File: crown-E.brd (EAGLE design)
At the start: 57.8 x 50.8 mm, 85 parts

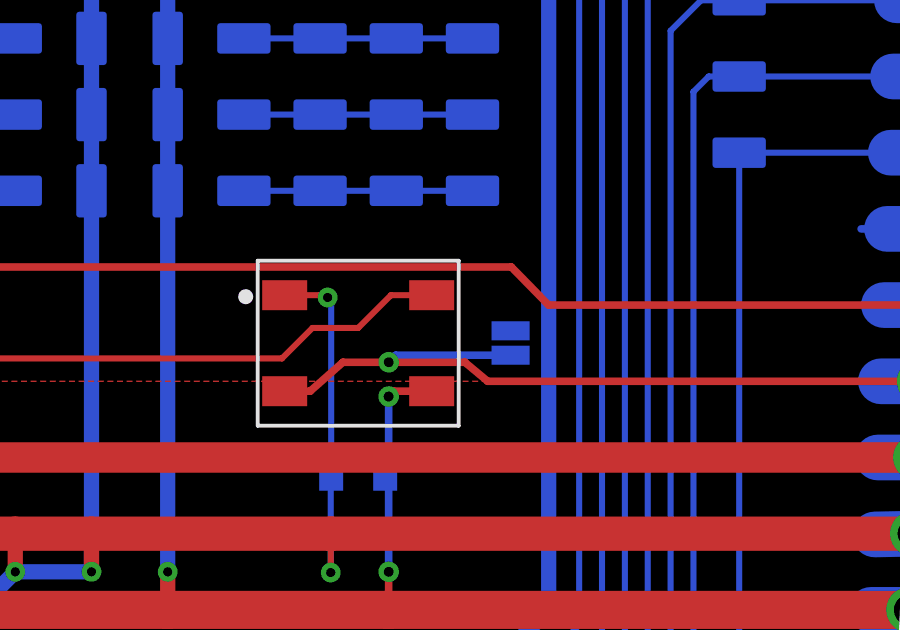
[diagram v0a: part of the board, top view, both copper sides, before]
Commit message: forgot a connection on skip-smd bits
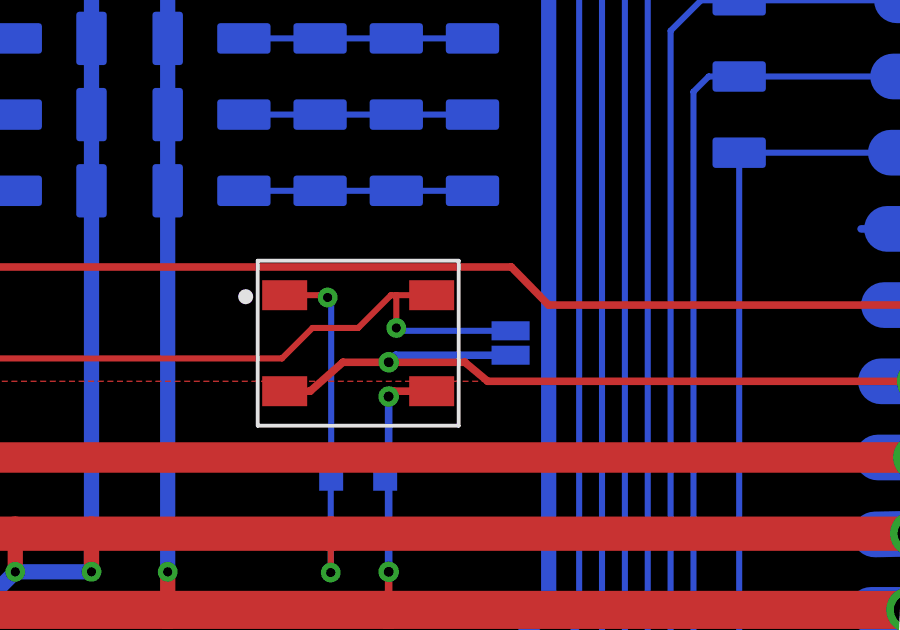
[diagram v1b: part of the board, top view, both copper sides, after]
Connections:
- net N$10: now also SKIP-SMD2.2
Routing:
- net N$10: track 28.2 -> 33.2 mm, vias 1 -> 2
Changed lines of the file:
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@@
 <grid distance="10" unitdist="mil" unit="mil" style="lines" multiple="5" display="yes" altdistance="1" altunitdist="mil" altunit="mil"/>
 <layers>
-<layer number="1" name="Top" color="4" fill="1" visible="no" active="yes"/>
-<layer number="16" name="Bottom" color="1" fill="1" visible="no" active="yes"/>
-<layer number="17" name="Pads" color="2" fill="1" visible="no" active="yes"/>
-<layer number="18" name="Vias" color="2" fill="1" visible="no" active="yes"/>
-<layer number="19" name="Unrouted" color="6" fill="1" visible="no" active="yes"/>
-<layer number="20" name="Dimension" color="15" fill="1" visible="no" active="yes"/>
-<layer number="21" name="tPlace" color="16" fill="1" visible="no" active="yes"/>
-<layer number="22" name="bPlace" color="14" fill="1" visible="no" active="yes"/>
-<layer number="23" name="tOrigins" color="15" fill="1" visible="no" active="yes"/>
-<layer number="24" name="bOrigins" color="15" fill="1" visible="no" active="yes"/>
+<layer number="1" name="Top" color="4" fill="1" visible="yes" active="yes"/>
+<layer number="16" name="Bottom" color="1" fill="1" visible="yes" active="yes"/>
+<layer number="17" name="Pads" color="2" fill="1" visible="yes" active="yes"/>
+<layer number="18" name="Vias" color="2" fill="1" visible="yes" active="yes"/>
+<layer number="19" name="Unrouted" color="6" fill="1" visible="yes" active="yes"/>
+<layer number="20" name="Dimension" color="15" fill="1" visible="yes" active="yes"/>
+<layer number="21" name="tPlace" color="16" fill="1" visible="yes" active="yes"/>
+<layer number="22" name="bPlace" color="14" fill="1" visible="yes" active="yes"/>
+<layer number="23" name="tOrigins" color="15" fill="1" visible="yes" active="yes"/>
+<layer number="24" name="bOrigins" color="15" fill="1" visible="yes" active="yes"/>
 <layer number="25" name="tNames" color="7" fill="1" visible="no" active="yes"/>
 <layer number="26" name="bNames" color="7" fill="1" visible="no" active="yes"/>
@@
 <layer number="28" name="bValues" color="7" fill="1" visible="no" active="yes"/>
 <layer number="29" name="tStop" color="7" fill="3" visible="yes" active="yes"/>
-<layer number="30" name="bStop" color="7" fill="6" visible="no" active="yes"/>
+<layer number="30" name="bStop" color="7" fill="6" visible="yes" active="yes"/>
 <layer number="31" name="tCream" color="7" fill="4" visible="no" active="yes"/>
 <layer number="32" name="bCream" color="7" fill="5" visible="no" active="yes"/>
@@
 <layer number="43" name="vRestrict" color="2" fill="10" visible="no" active="yes"/>
 <layer number="44" name="Drills" color="7" fill="1" visible="no" active="yes"/>
-<layer number="45" name="Holes" color="7" fill="1" visible="no" active="yes"/>
+<layer number="45" name="Holes" color="7" fill="1" visible="yes" active="yes"/>
 <layer number="46" name="Milling" color="3" fill="1" visible="no" active="yes"/>
 <layer number="47" name="Measures" color="7" fill="1" visible="no" active="yes"/>
@@
 <layer number="49" name="Reference" color="7" fill="1" visible="no" active="yes"/>
 <layer number="50" name="dxf" color="7" fill="1" visible="no" active="no"/>
-<layer number="51" name="tDocu" color="6" fill="1" visible="no" active="yes"/>
+<layer number="51" name="tDocu" color="6" fill="1" visible="yes" active="yes"/>
 <layer number="52" name="bDocu" color="7" fill="1" visible="no" active="yes"/>
 <layer number="53" name="tGND_GNDA" color="7" fill="9" visible="no" active="no"/>
@@
 <wire x1="36.576" y1="17.018" x2="38.1" y2="17.018" width="0.2032" layer="1"/>
 <wire x1="38.1" y1="17.018" x2="39.192" y2="18.11" width="0.2032" layer="1"/>
-<wire x1="39.192" y1="18.11" x2="40.55" y2="18.11" width="0.2032" layer="1"/>
+<wire x1="39.192" y1="18.11" x2="39.37" y2="18.11" width="0.2032" layer="1"/>
+<wire x1="39.37" y1="18.11" x2="40.55" y2="18.11" width="0.2032" layer="1"/>
 <wire x1="24.892" y1="16.3631" x2="24.7849" y2="16.256" width="0.2032" layer="16"/>
 <wire x1="24.7849" y1="16.256" x2="21.336" y2="16.256" width="0.2032" layer="16"/>
 <wire x1="21.336" y1="16.256" x2="21.082" y2="16.002" width="0.2032" layer="16"/>
 <via x="21.082" y="16.002" extent="1-16" drill="0.3048"/>
+<contactref element="SKIP-SMD2" pad="2"/>
+<wire x1="43.18" y1="16.9227" x2="39.4653" y2="16.9227" width="0.2032" layer="16"/>
+<wire x1="39.4653" y1="16.9227" x2="39.37" y2="17.018" width="0.2032" layer="16"/>
+<via x="39.37" y="17.018" extent="1-16" drill="0.3048"/>
+<wire x1="39.37" y1="17.018" x2="39.37" y2="18.11" width="0.2032" layer="1"/>
 </signal>
 <signal name="A0">

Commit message: fixed incorrect resistor value
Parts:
- moved PTH-END-NODE 30.8 mm to (13.7, 48.3), turned to 0 degrees
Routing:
- net PB1: track 60.4 -> 91.0 mm, vias 0 -> 1
- net N$4: track 69.9 -> 43.8 mm
- net VLIVE: track 291.8 -> 289.5 mm
- added copper zone on layer 1, net N$4
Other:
- board text added: "PIXEL LINE TERMINATION (((500 OHM RES))"
- board text added: "PIXEL LINE TERMINATION (500 OHM RES)"
- board text removed: "PIXEL LINE TERMINATION (150 OHM RES)"
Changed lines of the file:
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@@
 <text x="12.954" y="16.51" size="0.762" layer="22" font="vector" ratio="15" rot="MR90" align="bottom-center">PIXEL LINE
 TERMINATION
-(150 OHM RES)</text>
+(500 OHM RES)</text>
 <text x="4.572" y="7.62" size="0.762" layer="22" font="vector" ratio="15" rot="MR0" align="center-right">GND</text>
 <text x="4.572" y="5.08" size="0.762" layer="22" font="vector" ratio="15" rot="MR0" align="center-right">VBAT</text>
@@
 <text x="8.636" y="15.24" size="0.762" layer="22" font="vector" ratio="15" rot="MR0" align="center-right">SMD DO</text>
 <text x="8.636" y="17.78" size="0.762" layer="22" font="vector" ratio="15" rot="MR0" align="center-right">PTH DI</text>
-<text x="8.636" y="20.32" size="0.762" layer="22" font="vector" ratio="15" rot="MR0" align="center-right">PTH DO</text>
 <text x="53.848" y="7.62" size="0.762" layer="22" font="vector" ratio="15" rot="MR180" align="center-right">GND</text>
 <text x="53.848" y="5.08" size="0.762" layer="22" font="vector" ratio="15" rot="MR180" align="center-right">VBAT</text>
@@
 <vertex x="0" y="50.8"/>
 </polygon>
+<text x="13.716" y="44.196" size="0.762" layer="22" font="vector" ratio="15" rot="MR0" align="bottom-center">PIXEL LINE
+TERMINATION
+(((500 OHM RES))</text>
 </plain>
 <attributes>
@@
 <attribute name="VALUE" x="18.288" y="54.0766" size="0.4064" layer="28" rot="MR90"/>
 </element>
-<element name="PTH-END-NODE" library="SparkFun-Passives" package="0805" value="300-500 OHM" x="4.826" y="18.796" smashed="yes" rot="MR90">
-<attribute name="NAME" x="-6.0325" y="14.478" size="0.762" layer="26" ratio="15" rot="MR90"/>
-<attribute name="VALUE" x="-6.985" y="15.494" size="0.762" layer="28" ratio="15" rot="MR90"/>
+<element name="PTH-END-NODE" library="SparkFun-Passives" package="0805" value="300-500 OHM" x="13.716" y="48.26" smashed="yes" rot="MR0">
+<attribute name="NAME" x="18.034" y="37.4015" size="0.762" layer="26" ratio="15" rot="MR0"/>
+<attribute name="VALUE" x="17.018" y="36.449" size="0.762" layer="28" ratio="15" rot="MR0"/>
 </element>
 <element name="SMD-END-NODE" library="SparkFun-Passives" package="0805" value="300-500 OHM" x="4.826" y="13.97" smashed="yes" rot="MR90">
@@
 <wire x1="31.75" y1="21.59" x2="31.75" y2="8.89" width="0.508" layer="16"/>
 <wire x1="19.685" y1="55.9926" x2="19.939" y2="55.9926" width="0.2032" layer="16"/>
-<polygon width="0.2032" layer="1" isolate="0.254" orphans="yes">
+<polygon width="0.2032" layer="1" isolate="0.254" orphans="yes" rank="2">
 <vertex x="0.254" y="15.24"/>
 <vertex x="0" y="51.308"/>
@@
 <wire x1="43.942" y1="49.022" x2="44.323" y2="52.07" width="0" layer="19" extent="16-16"/>
 <wire x1="1.7272" y1="7.62" x2="1.778" y2="7.62" width="0" layer="19" extent="1-1"/>
+<wire x1="20.193" y1="55.8546" x2="31.75" y2="45.466" width="0" layer="19" extent="16-16"/>
 <wire x1="14.986" y1="59.6646" x2="14.859" y2="57.1246" width="0" layer="19" extent="16-16"/>
 </signal>
@@
 <wire x1="29.21" y1="8.89" x2="29.21" y2="10.16" width="0.508" layer="1"/>
 <contactref element="U$2" pad="P$17"/>
-<wire x1="0.254" y1="43.18" x2="6.096" y2="43.18" width="0.508" layer="16"/>
-<wire x1="6.096" y1="43.18" x2="13.716" y2="50.8" width="0.508" layer="16"/>
+<wire x1="0.254" y1="43.18" x2="11.43" y2="43.18" width="0.508" layer="16"/>
+<wire x1="11.43" y1="43.18" x2="13.716" y2="45.72" width="0.508" layer="16"/>
+<wire x1="13.716" y1="45.72" x2="13.716" y2="50.8" width="0.508" layer="16"/>
 <wire x1="16.267" y1="50.7746" x2="19.5" y2="54.0076" width="0.508" layer="16"/>
 <wire x1="19.5" y1="54.0076" x2="19.685" y2="54.1926" width="0.508" layer="16"/>
@@
 <wire x1="13.716" y1="50.8" x2="16.2416" y2="50.8" width="0.508" layer="16"/>
 <wire x1="16.2416" y1="50.8" x2="16.267" y2="50.7746" width="0.508" layer="16"/>
-<wire x1="6.096" y1="43.18" x2="12.192" y2="43.18" width="0.508" layer="16"/>
+<wire x1="11.43" y1="43.18" x2="12.192" y2="43.18" width="0.508" layer="16"/>
 <wire x1="12.192" y1="43.18" x2="16.002" y2="39.37" width="0.508" layer="16"/>
 <wire x1="16.002" y1="39.37" x2="16.002" y2="9.398" width="0.508" layer="16"/>
@@
 <contactref element="PTH1" pad="P$4"/>
 <contactref element="U$2" pad="P$8"/>
-<wire x1="4.456" y1="20.32" x2="4.4767" y2="20.32" width="0.254" layer="16"/>
 <wire x1="12.192" y1="60.1726" x2="12.065" y2="60.4266" width="0.254" layer="16"/>
 <wire x1="12.446" y1="54.8386" x2="12.319" y2="54.8386" width="0.254" layer="16"/>
 <contactref element="PTH-END-NODE" pad="2"/>
-<wire x1="1.1938" y1="20.32" x2="2.54" y2="20.32" width="0.254" layer="16"/>
-<wire x1="2.54" y1="20.32" x2="4.456" y2="20.32" width="0.254" layer="16"/>
-<wire x1="4.456" y1="20.32" x2="4.826" y2="19.696" width="0.254" layer="16"/>
 <wire x1="12.446" y1="58.3946" x2="12.446" y2="59.9186" width="0.2032" layer="16"/>
 <wire x1="12.319" y1="60.0456" x2="12.192" y2="60.1726" width="0.2032" layer="16"/>
-<wire x1="2.54" y1="20.32" x2="0" y2="20.32" width="0.2032" layer="16"/>
-<wire x1="0" y1="20.32" x2="-1.27" y2="21.59" width="0.2032" layer="16"/>
-<wire x1="-1.27" y1="21.59" x2="-1.27" y2="48.26" width="0.2032" layer="16"/>
 <contactref element="U$2" pad="P$19"/>
 <wire x1="0.0508" y1="48.26" x2="3.81" y2="48.26" width="0.2032" layer="16"/>
-<wire x1="-1.27" y1="48.26" x2="0.0508" y2="48.26" width="0.2032" layer="16"/>
 <wire x1="3.81" y1="48.26" x2="5.08" y2="50.8" width="0.2032" layer="16"/>
 <wire x1="5.08" y1="50.8" x2="11.811" y2="58.3946" width="0.2032" layer="16"/>
@@
 <wire x1="18.415" y1="62.2046" x2="19.431" y2="61.1886" width="0.2032" layer="16"/>
 <wire x1="19.431" y1="61.1886" x2="19.431" y2="59.5693" width="0.2032" layer="16"/>
+<wire x1="-1.27" y1="48.26" x2="1.016" y2="48.26" width="0.2032" layer="1"/>
+<wire x1="2.54" y1="20.32" x2="1.1938" y2="20.32" width="0.2032" layer="1"/>
+<polygon width="0.2032" layer="1">
+<vertex x="-0.762" y="20.32"/>
+<vertex x="2.54" y="20.32"/>
+<vertex x="1.27" y="48.26"/>
+<vertex x="-1.27" y="48.26"/>
+</polygon>
 <wire x1="12.446" y1="58.3946" x2="12.446" y2="54.8386" width="0" layer="19" extent="16-16"/>
+<wire x1="12.816" y1="48.26" x2="12.446" y2="54.8386" width="0.2032" layer="16"/>
 </signal>
 <signal name="HALF-VBAT">
@@
 <contactref element="U$2" pad="P$7"/>
 <contactref element="PTH-END-NODE" pad="1"/>
-<wire x1="3.948" y1="17.78" x2="3.9569" y2="17.78" width="0.254" layer="16"/>
 <wire x1="56.9214" y1="17.78" x2="44.45" y2="17.78" width="0.254" layer="1"/>
 <wire x1="44.45" y1="17.78" x2="43.2054" y2="19.05" width="0.254" layer="1"/>
-<wire x1="43.2054" y1="19.05" x2="15.24" y2="19.05" width="0.254" layer="1"/>
+<wire x1="43.2054" y1="19.05" x2="20.574" y2="19.05" width="0.254" layer="1"/>
+<wire x1="20.574" y1="19.05" x2="15.24" y2="19.05" width="0.254" layer="1"/>
 <wire x1="1.27" y1="17.78" x2="13.97" y2="17.78" width="0.254" layer="1"/>
 <wire x1="13.97" y1="17.78" x2="15.24" y2="19.05" width="0.254" layer="1"/>
-<wire x1="1.27" y1="17.78" x2="3.948" y2="17.78" width="0.254" layer="16"/>
-<wire x1="3.948" y1="17.78" x2="4.826" y2="17.896" width="0.254" layer="16"/>
-<wire x1="4.942" y1="17.78" x2="4.826" y2="17.896" width="0.2032" layer="16"/>
+<wire x1="20.574" y1="19.05" x2="20.574" y2="18.288" width="0.2032" layer="1"/>
+<wire x1="20.574" y1="18.288" x2="17.272" y2="20.32" width="0.2032" layer="16"/>
+<wire x1="17.272" y1="20.32" x2="17.272" y2="47.244" width="0.2032" layer="16"/>
+<wire x1="17.272" y1="47.244" x2="16.256" y2="48.26" width="0.2032" layer="16"/>
+<wire x1="16.256" y1="48.26" x2="14.986" y2="48.26" width="0.2032" layer="16"/>
+<via x="20.574" y="18.288" extent="1-16" drill="0.3048"/>
+<wire x1="14.986" y1="48.26" x2="14.616" y2="48.26" width="0" layer="19" extent="16-16"/>
 </signal>
 <signal name="PB5">
